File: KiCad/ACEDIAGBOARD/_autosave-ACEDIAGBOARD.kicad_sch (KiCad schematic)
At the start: 47 parts, among them J1 Conn_01x16, J2 Conn_01x08, J3 Conn_01x06, J4 Conn_01x08, J5 Conn_01x10, SW1 STEP, SW2 RUN/STEP, SW3 RESET, U1 NE555P, U2 74LS00, U3 74LS74, U4 74LS241, U5 74LS241, U6 74LS241, U7 74LS241, U8 74LS241

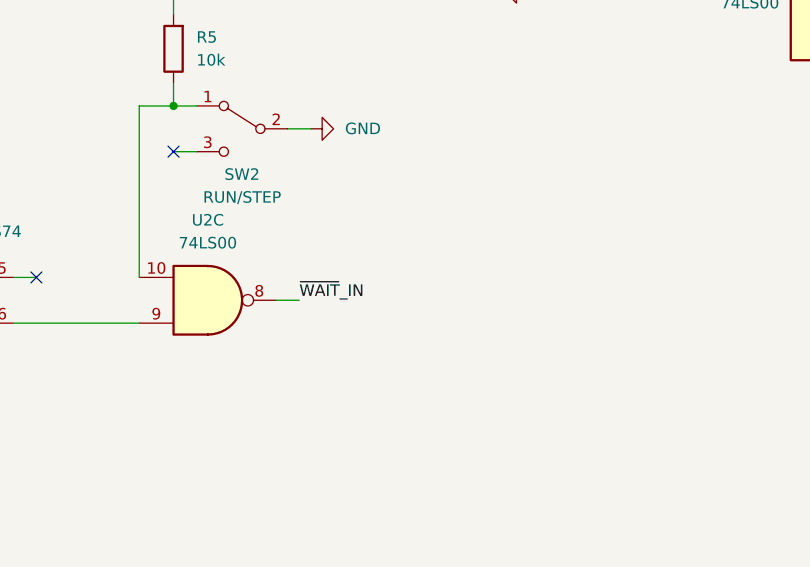
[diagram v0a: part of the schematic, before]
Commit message: Consolidation with increased configuration of speed and Int Routing to allow Orginal ACE ROM.
Signed-off-by: John Bradley <flypie@rocketmail.com>
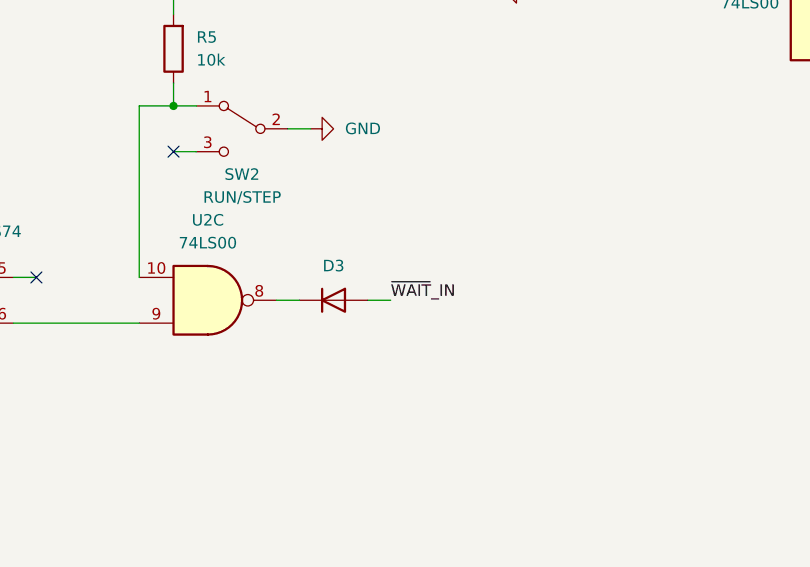
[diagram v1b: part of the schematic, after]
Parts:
- added D3: 1N4148, Diode_THT:D_DO-35_SOD27_P2.54mm_Vertical_AnodeUp, symbol Diode:1N4148
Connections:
- net ~{WAIT}_IN: now also D3.2 (A); no longer U2.8
- new net: D3.1 (K), U2.8
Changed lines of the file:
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@@
     (stroke (width 0) (type default) (color 0 0 0 0))
   )
+  (wire (pts (xy 156.21 161.29) (xy 153.67 161.29))
+    (stroke (width 0) (type default) (color 0 0 0 0))
+  )
   (wire (pts (xy 299.72 170.18) (xy 297.18 170.18))
     (stroke (width 0) (type default) (color 0 0 0 0))
@@
     (stroke (width 0) (type default) (color 0 0 0 0))
   )
-  (wire (pts (xy 156.21 161.29) (xy 153.67 161.29))
+  (wire (pts (xy 166.37 161.29) (xy 163.83 161.29))
     (stroke (width 0) (type default) (color 0 0 0 0))
   )
@@
     (effects (font (size 1.27 1.27)) (justify right bottom))
   )
-  (label "~{WAIT}_IN" (at 156.21 161.29 0)
+  (label "~{WAIT}_IN" (at 166.37 161.29 0)
     (effects (font (size 1.27 1.27)) (justify left bottom))
   )
@@
     (pin "1")
   )
+  (symbol (lib_id "Diode:1N4148") (at 160.02 161.29 0) (unit 1)
+    (in_bom yes) (on_board yes) (fields_autoplaced)
+    (property "Reference" "D3" (id 0) (at 160.02 157.48 0))
+    (property "Value" "1N4148" (id 1) (at 160.02 159.131 90)
+      (effects (font (size 1.27 1.27)) (justify left) hide)
+    )
+    (property "Footprint" "Diode_THT:D_DO-35_SOD27_P2.54mm_Vertical_AnodeUp" (id 2) (at 160.02 165.735 0)
+      (effects (font (size 1.27 1.27)) hide)
+    )
+    (property "Datasheet" "https://assets.nexperia.com/documents/data-sheet/1N4148_1N4448.pdf" (id 3) (at 160.02 161.29 0)
+      (effects (font (size 1.27 1.27)) hide)
+    )
+    (property "Manufacturer_Name" "ON Semiconductor" (id 4) (at 160.02 161.29 0)
+      (effects (font (size 1.27 1.27)) hide)
+    )
+    (property "Manufacturer_Part_Number" "1N4148" (id 5) (at 160.02 161.29 0)
+      (effects (font (size 1.27 1.27)) hide)
+    )
+    (pin "1")
+    (pin "2")
+  )
   (symbol (lib_id "74xx-FIX:74LS241") (at 312.42 40.64 0) (unit 1)
     (in_bom yes) (on_board yes) (fields_autoplaced)
@@
       (reference "D2") (unit 1) (value "LED") (footprint "LED_THT:LED_D5.0mm_Clear")
     )
+    (path "/9eeaab67-f5c9-46a4-85eb-fea522899fc5"
+      (reference "D3") (unit 1) (value "1N4148") (footprint "Diode_THT:D_DO-35_SOD27_P2.54mm_Vertical_AnodeUp")
+    )
     (path "/00000000-0000-0000-0000-00005fb07ac0"
